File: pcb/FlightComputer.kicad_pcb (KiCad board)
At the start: 2 copper layers, 22.9 x 63.5 mm, 79 parts, among them J1 USB4105-GF-A, J2 MOTOR L, J3 MOTOR R, J4 LED L, J7 SERVO R, J8 SERVO R, Q1 DMG3415U, Q2 Si2319CDS, Q3 Si2319CDS, Q4 MMBT3904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

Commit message: Rotate servos pinouts
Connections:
- J7 pad 1: IO1 -> GND
- J7 pad 3: GND -> IO1
- J8 pad 1: IO6 -> GND
- J8 pad 3: GND -> IO6
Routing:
- net IO6: track 21.4 -> 15.7 mm
- net IO1: track 15.5 -> 12.9 mm
- net GND: vias 220 -> 221
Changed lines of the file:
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@@
 			(layers "*.Cu" "*.Mask")
 			(remove_unused_layers no)
-			(net 68 "IO1")
+			(net 1 "GND")
 			(pinfunction "Pin_1")
 			(pintype "passive")
@@
 			(layers "*.Cu" "*.Mask")
 			(remove_unused_layers no)
-			(net 1 "GND")
+			(net 68 "IO1")
 			(pinfunction "Pin_3")
 			(pintype "passive")
@@
 			(layers "*.Cu" "*.Mask")
 			(remove_unused_layers no)
-			(net 28 "IO6")
+			(net 1 "GND")
 			(pinfunction "Pin_1")
 			(pintype "passive")
@@
 			(layers "*.Cu" "*.Mask")
 			(remove_unused_layers no)
-			(net 1 "GND")
+			(net 28 "IO6")
 			(pinfunction "Pin_3")
 			(pintype "passive")
@@
 	)
 	(via
+		(at 151.0284 118)
+		(size 0.6)
+		(drill 0.3)
+		(layers "F.Cu" "B.Cu")
+		(free yes)
+		(net 1)
+	)
+	(via
 		(at 154.4 103.85)
 		(size 0.6)
@@
 	)
 	(segment
-		(start 140.739 73.745)
-		(end 140.65 73.834)
-		(width 0.508)
-		(layer "F.Cu")
-		(net 2)
-	)
-	(segment
 		(start 148.092 87.934)
 		(end 148.442 87.934)
@@
 	)
 	(segment
-		(start 159 92.5)
-		(end 157.75 93.75)
-		(width 0.1524)
-		(layer "B.Cu")
-		(net 28)
-	)
-	(segment
-		(start 150.8794 83.0794)
-		(end 158.2634 83.0794)
+		(start 149.7 81.9)
+		(end 150.8794 83.0794)
 		(width 0.1524)
 		(layer "B.Cu")
@@
 	)
 	(segment
-		(start 158.2634 83.0794)
-		(end 159 83.816)
+		(start 157.25 83.0794)
+		(end 157.75 83.5794)
 		(width 0.1524)
 		(layer "B.Cu")
@@
 	)
 	(segment
-		(start 159 83.816)
-		(end 159 92.5)
+		(start 150.8794 83.0794)
+		(end 157.25 83.0794)
 		(width 0.1524)
 		(layer "B.Cu")
@@
 	)
 	(segment
-		(start 149.7 81.9)
-		(end 150.8794 83.0794)
+		(start 157.75 83.5794)
+		(end 157.75 89.75)
 		(width 0.1524)
 		(layer "B.Cu")
@@
 	)
 	(segment
-		(start 144.082 81.9)
-		(end 144.082 81.1)
-		(width 0.1524)
-		(layer "F.Cu")
-		(net 68)
-	)
-	(segment
-		(start 143.1 90)
-		(end 142.25 90)
+		(start 141.8398 89.75)
+		(end 138.5 89.75)
 		(width 0.1524)
 		(layer "F.Cu")
@@
 	)
 	(segment
-		(start 142.25 90)
-		(end 138.5 93.75)
+		(start 144.082 81.9)
+		(end 144.082 81.1)
 		(width 0.1524)
 		(layer "F.Cu")
@@
 	)
 	(via
-		(at 143.1 90)
+		(at 141.8398 89.75)
 		(size 0.6)
 		(drill 0.3)
@@
 	)
 	(segment
-		(start 143.1 90)
-		(end 144.082 89.018)
+		(start 141.8398 89.75)
+		(end 144.082 87.5078)
 		(width 0.1524)
 		(layer "B.Cu")
@@
 	)
 	(segment
-		(start 144.082 89.018)
+		(start 144.082 87.5078)
 		(end 144.082 81.9)
 		(width 0.1524)
@@
 		(polygon
 			(pts
-				(xy 155 94.25) (xy 140.75 94.25) (xy 140.75 83) (xy 158.5 83) (xy 158.5 88.5976) (xy 155 88.5952)
+				(xy 155 94.25) (xy 140.75 94.25) (xy 140.75 83) (xy 157.5 83) (xy 157.5 88.25) (xy 155 88.25)
 			)
 		)

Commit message: Remove barometer
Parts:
- removed C22, C23: 100nF 10V, Capacitor_SMD:C_0402_1005Metric
- removed U1: BMP388, Package_LGA:Rohm_MLGA010V020A_LGA-10_2x2mm_P0.45mm_LayoutBorder2x3y
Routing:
- net +3V3: track 60.8 -> 55.7 mm, vias 15 -> 13
- net IO8_SCL: track 28.7 -> 25.8 mm
- net IO10_SDA: track 28.7 -> 26.3 mm

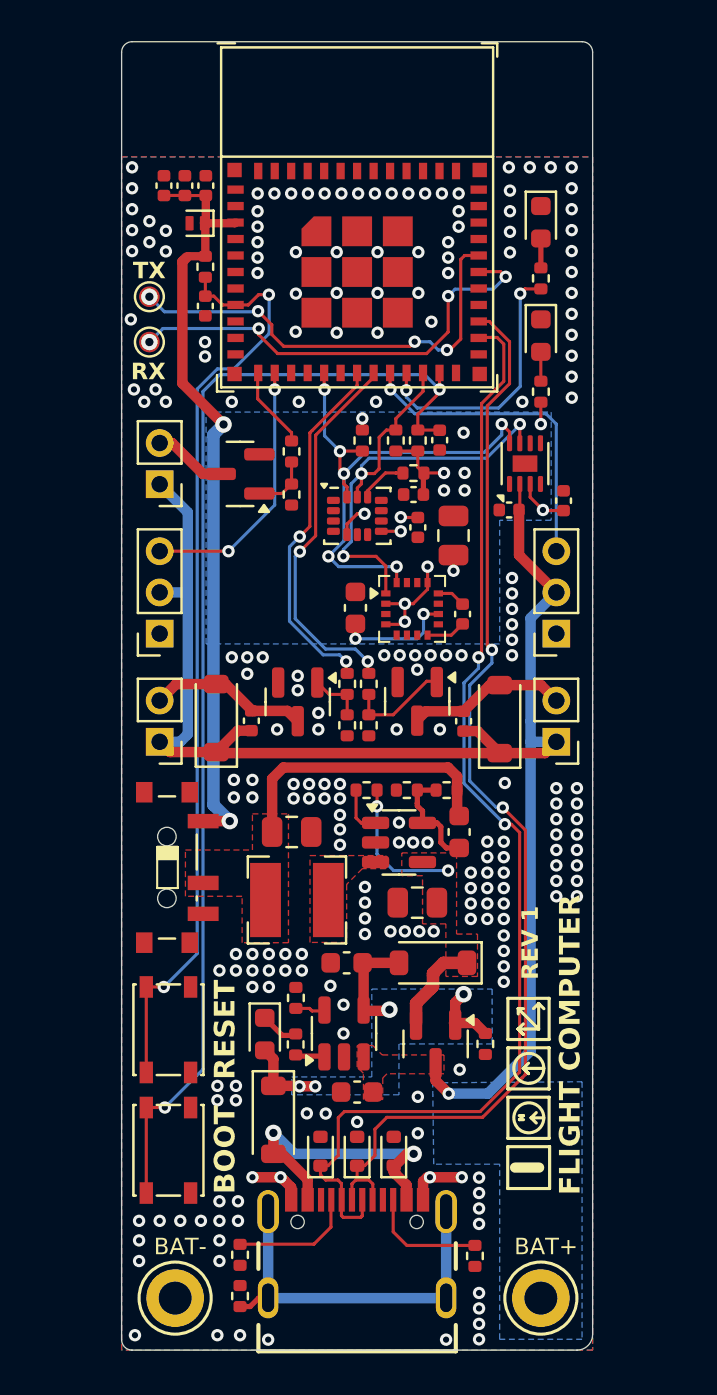
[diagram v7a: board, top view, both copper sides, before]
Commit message: Reduce board size
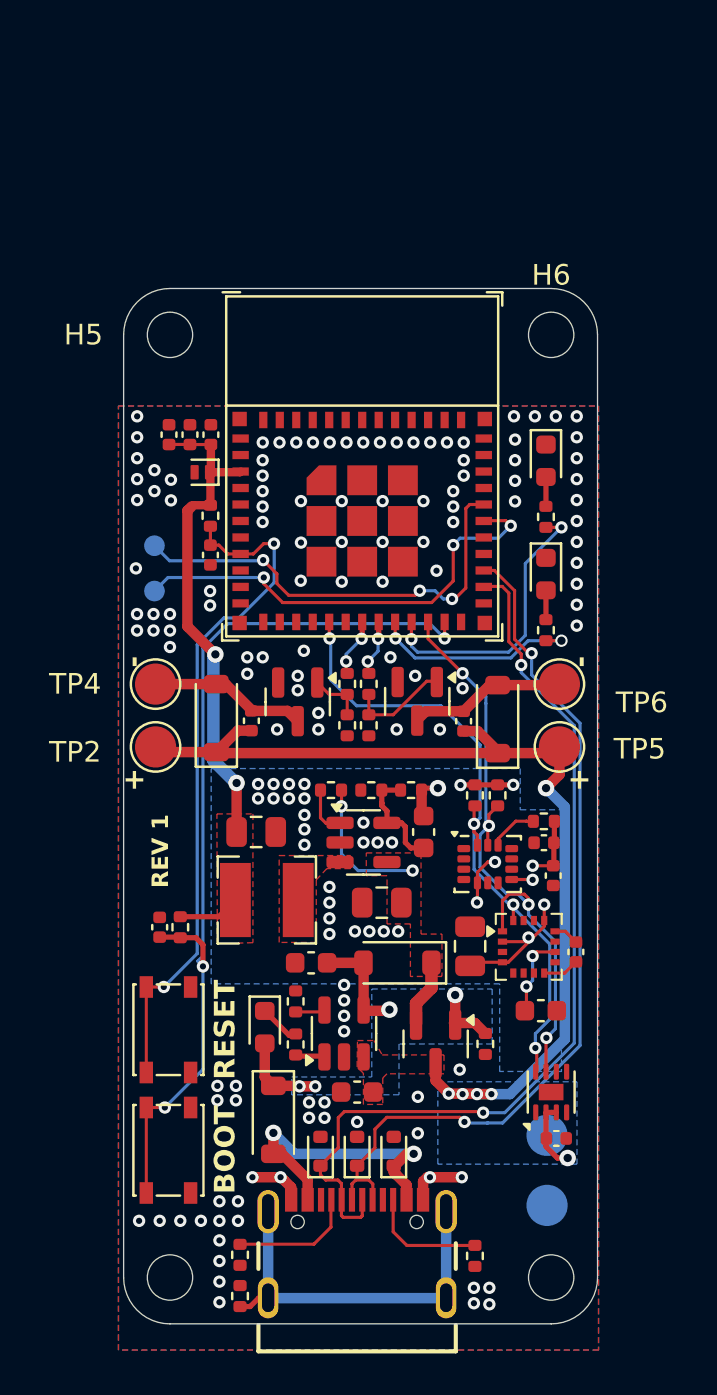
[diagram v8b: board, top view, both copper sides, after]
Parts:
- removed C17: 1uF 16V, Capacitor_SMD:C_0402_1005Metric
- removed J2: MOTOR L, Connector_PinHeader_2.00mm:PinHeader_1x02_P2.00mm_Vertical
- removed J3: MOTOR R, Connector_PinHeader_2.00mm:PinHeader_1x02_P2.00mm_Vertical
- removed J4: LED L, Connector_PinHeader_2.00mm:PinHeader_1x02_P2.00mm_Vertical
- removed J7, J8: SERVO R, Connector_PinSocket_2.00mm:PinSocket_1x03_P2.00mm_Vertical
- removed Q4: MMBT3904, Package_TO_SOT_SMD:SOT-23
- removed R22: 470R 1%, Resistor_SMD:R_0402_1005Metric
- removed R23: 10kR 1%, Resistor_SMD:R_0402_1005Metric
- removed SW3: SW_DPDT_x2, Rust_Board:SW_SPDT_PCM12
- added H3: MountingHole, MountingHole:MountingHole_2.2mm_M2_DIN965, F.Cu at (157.5, 125.0)
- added H4: MountingHole, MountingHole:MountingHole_2.2mm_M2_DIN965, F.Cu at (139.0, 125.0)
- added H5: MountingHole, MountingHole:MountingHole_2.2mm_M2_DIN965, F.Cu at (139.0, 79.2)
- added H6: MountingHole, MountingHole:MountingHole_2.2mm_M2_DIN965, F.Cu at (157.5, 79.2)
- added TP2: TestPoint, TestPoint:TestPoint_Pad_D2.0mm, F.Cu at (138.3, 99.2)
- added TP4: TestPoint, TestPoint:TestPoint_Pad_D2.0mm, F.Cu at (138.3, 96.2)
- added TP5: TestPoint, TestPoint:TestPoint_Pad_D2.0mm, F.Cu at (157.9, 99.2)
- added TP6: TestPoint, TestPoint:TestPoint_Pad_D2.0mm, F.Cu at (157.9, 96.2)
- H1, H2: footprint TestPoint:TestPoint_Keystone_5005-5009_Compact -> TestPoint:TestPoint_Pad_D2.0mm; moved to B.Cu
- TP1, TP3: moved to B.Cu
- moved C18 30.6 mm to (157.8, 118.2), turned to 0 degrees
- moved U7 30.5 mm to (157.5, 116.0)
- moved C14 27.3 mm to (138.5, 108.0), turned to -90 degrees
- moved R19 26.3 mm to (139.5, 108.0), turned to -90 degrees
- moved C19 21.5 mm to (157.0, 112.0), turned to 0 degrees
- moved C20 20.0 mm to (153.6, 108.9)
- moved H2 18.6 mm to (157.3, 121.5), turned to 180 degrees
- moved C2 18.1 mm to (157.6, 105.5)
- moved R18 18.1 mm to (153.8, 101.6)
- moved C4 18.0 mm to (157.2, 103.9)
- moved R7 18.0 mm to (157.1, 102.9)
- moved U2 18.0 mm to (154.4, 104.9)
- moved R17 17.9 mm to (154.9, 101.6), turned to -90 degrees
- moved U9 17.3 mm to (156.4, 108.9)
- moved C21 17.3 mm to (158.7, 109.2)
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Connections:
- C6 pad 1: /POWER -> +3V3
- C7 pad 1: /POWER -> +3V3
- L1 pad 2: /POWER -> +3V3
- R10 pad 1: +3V3 -> IO6
- R2 pad 1: /POWER -> +3V3
- U3 pad 12: IO0 -> unconnected-(U3-GPIO0/ADC1_CH0/XTAL_32K_P-Pad12)
- U3 pad 13: IO1 -> unconnected-(U3-GPIO1/ADC1_CH1/XTAL_32K_N-Pad13)
- U7 pad 3: +3V3 -> +BATT
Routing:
- net +BATT: track 76.5 -> 50.8 mm, vias 1 -> 6
- net IO5: track 18.3 -> 2.52 mm
- net IO4: track 17.7 -> 2.98 mm
- net /POWER: track 14.5 -> 0.00 mm
- net IO1: track 12.9 -> 0.00 mm, vias 2 -> 0
- net CHIP_PU: track 45.5 -> 33.5 mm
- net IO9_BOOT: track 56.9 -> 45.0 mm, vias 2 -> 3
- net USB_D-: track 56.6 -> 45.4 mm
- net USB_D+: track 53.9 -> 42.7 mm
- net +3V3: track 55.7 -> 46.8 mm, vias 13 -> 11
- net IO10_SDA: track 26.3 -> 32.2 mm, vias 6 -> 4
- net IO6: track 15.7 -> 10.4 mm, vias 1 -> 2
- net IO8_SCL: track 25.8 -> 30.6 mm, vias 3 -> 4
- net IO0: track 4.05 -> 0.00 mm
- net Net-(J4-Pin_2): track 3.98 -> 0.00 mm
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- added copper zone on F.Cu, net +3V3
- removed copper zone on F.Cu, net /POWER
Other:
- board size 22.9 x 63.5 mm -> 23 x 50.2 mm
- board text added: "+"
- board text added: "2024-11-28"
- board text added: "B+"
- board text added: "B-"
- board text added: "ESP32-C3-Plane"
- board text added: "PAPER WINGS"
- board text added: "Rev 0.2"
- board text removed: "2022-04-27"
- board text removed: "BAT+"
- board text removed: "BAT-"
- board text removed: "ESP32-C3-DevKit-RUST-1"
- board text removed: "ESPRESSIF SYSTEMS"
- board text removed: "Rev 1.2a"
